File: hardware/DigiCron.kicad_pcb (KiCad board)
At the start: 2 copper layers, 36 x 36 mm, 11 parts, among them J100 Conn_Receptacle_2P, U100 MDBT50Q-U1MV2, U101 HCMS-3917, U102 HCMS-3917, U103 LTR-390UV-01, U104 ADXL345BCCZ-RL, U105 BME280, X100 12401598E4#2A

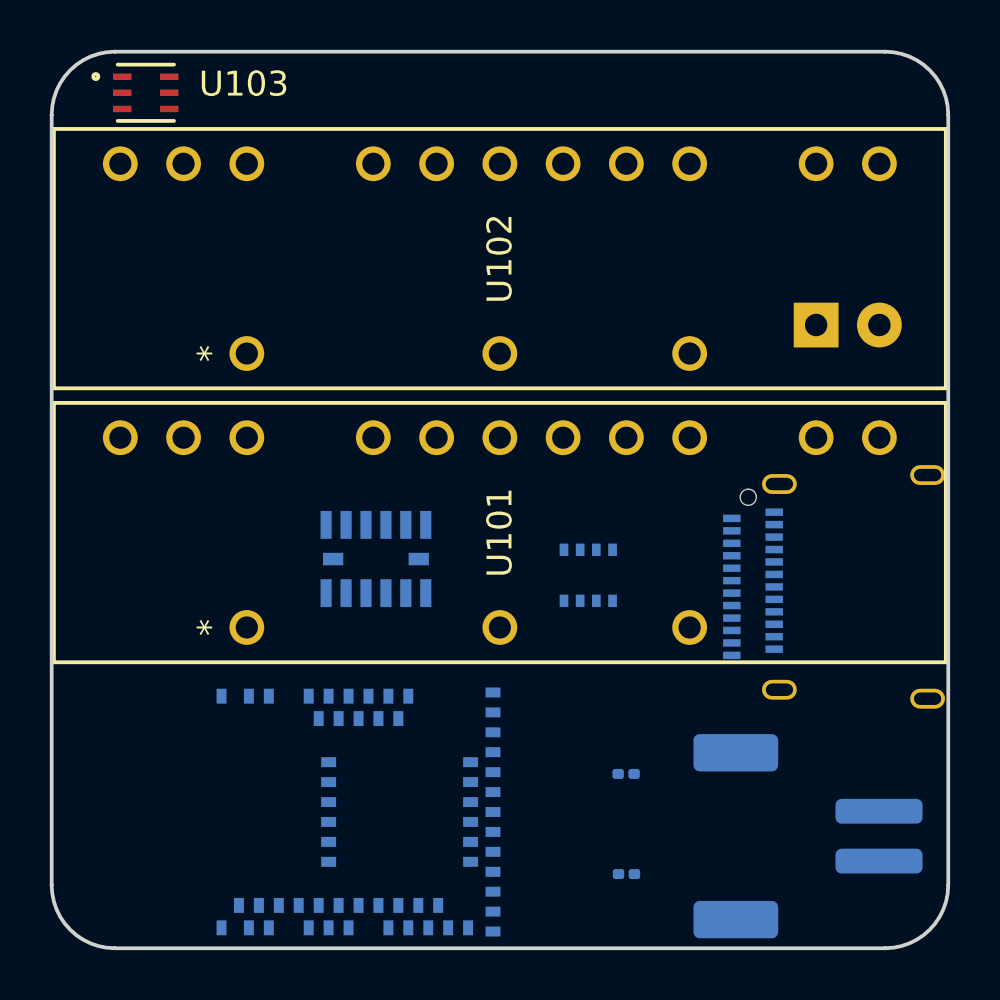
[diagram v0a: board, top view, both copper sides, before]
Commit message: Replace displays with 5V versions (due to supply availability) and add power management ICs
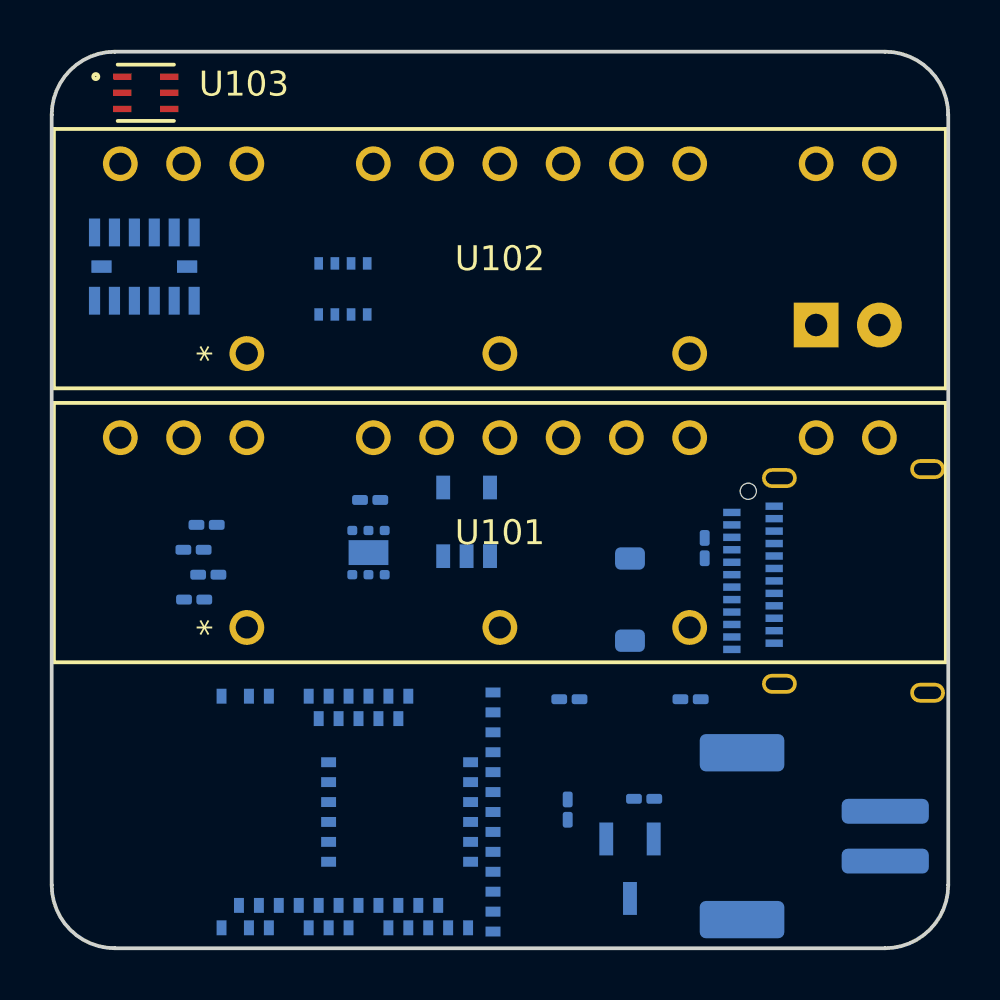
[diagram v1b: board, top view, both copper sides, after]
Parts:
- removed J100: Conn_Receptacle_2P, Connector_JST:JST_PH_S2B-PH-SM4-TB_1x02-1MP_P2.00mm_Horizontal
- removed R100, R101: 5.1K, Resistor_SMD:R_0201_0603Metric
- removed X100: 12401598E4#2A, USB-C:12401598E4#2A
- added C200: 10u, Capacitor_SMD:C_0201_0603Metric_Pad0.64x0.40mm_HandSolder, B.Cu at (203.7, 96.0)
- added C201: 10u, Capacitor_SMD:C_0201_0603Metric_Pad0.64x0.40mm_HandSolder, B.Cu at (186.1, 85.0)
- added C202: 10u, Capacitor_SMD:C_0201_0603Metric_Pad0.64x0.40mm_HandSolder, B.Cu at (185.6, 86.0)
- added C203: 10u, Capacitor_SMD:C_0201_0603Metric_Pad0.64x0.40mm_HandSolder, B.Cu at (186.2, 87.0)
- added C204: 10u, Capacitor_SMD:C_0201_0603Metric_Pad0.64x0.40mm_HandSolder, B.Cu at (185.6, 88.0)
- added D200: MBR0540, Diode_SMD:D_SOD-123, B.Cu at (203.1, 88.0)
- added J200: Conn_Receptacle_2P, Connector_JST:JST_PH_S2B-PH-SM4-TB_1x02-1MP_P2.00mm_Horizontal, B.Cu at (210.5, 97.5)
- added L200: 2.2u, Inductor_SMD:L_0201_0603Metric_Pad0.64x0.40mm_HandSolder, B.Cu at (192.7, 84.0)
- added Q200: AO3401A, AO3401A:SOT-23-3L_AOS, B.Cu at (203.1, 98.8)
- added R200: 5.1K, Resistor_SMD:R_0201_0603Metric_Pad0.64x0.40mm_HandSolder, B.Cu at (206.1, 86.0)
- added R201: 5.1K, Resistor_SMD:R_0201_0603Metric_Pad0.64x0.40mm_HandSolder, B.Cu at (205.6, 92.0)
- added R202: 100K, Resistor_SMD:R_0201_0603Metric_Pad0.64x0.40mm_HandSolder, B.Cu at (200.6, 96.5)
- added R203: 100K, Resistor_SMD:R_0201_0603Metric_Pad0.64x0.40mm_HandSolder, B.Cu at (200.7, 92.0)
- added U200: RT9080-33GJ5, RT9080:TSOT-23-5_RIT, B.Cu at (196.6, 84.9)
- added U201: TPS610997DRV, Package_SON:WSON-6-1EP_2x2mm_P0.65mm_EP1x1.6mm, B.Cu at (192.6, 86.2)
- added X200: 12401598E4#2A, USB-C:12401598E4#2A, B.Cu at (207.9, 87.3)
- moved U105 15.1 mm to (191.6, 75.6)
- moved U104 15.0 mm to (183.6, 74.7), turned to 90 degrees
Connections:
- net /A0 renamed A0
- net /A1 renamed A1
- net /A2 renamed A2
- net /A3 renamed A3
- net /A4 renamed A4
- net /A5 renamed A5
- net /ADPS_IRQ renamed ADPS_IRQ
- net /AREF renamed AREF
- net /D2 renamed D2
- net /HCMS_BLANK renamed HCMS_BLANK
- net /HCMS_CE renamed HCMS_CE
- net /HCMS_CLOCK renamed HCMS_CLOCK
- net /HCMS_DATA_IN renamed HCMS_DATA_IN
- net /HCMS_DATA_SHARE renamed HCMS_DATA_SHARE
- net /HCMS_RESET renamed HCMS_RESET
- net /HCMS_RS renamed HCMS_RS
- net /IR_IN renamed IR_IN
- net /JOY_BACK renamed JOY_BACK
- net /JOY_DOWN renamed JOY_DOWN
- net /JOY_HOME renamed JOY_HOME
- net /JOY_LEFT renamed JOY_LEFT
- net /JOY_RIGHT renamed JOY_RIGHT
- net /JOY_SELECT renamed JOY_SELECT
- net /JOY_UP renamed JOY_UP
- net /LED renamed LED
- net /MISO renamed MISO
- net /MOSI renamed MOSI
- net /QSPI_D0 renamed QSPI_D0
- net /QSPI_D1 renamed QSPI_D1
- net /QSPI_D2 renamed QSPI_D2
- net /QSPI_D3 renamed QSPI_D3
- net /QSPI_SCK renamed QSPI_SCK
- net /RESET renamed RESET
- net /RXD renamed RXD
- net /SCK renamed SCK
- net /SCL renamed SCL
- net /SDA renamed SDA
- net /SWCLK renamed SWCLK
- net /SWDIO renamed SWDIO
- net /TXD renamed TXD
- net /VDIV renamed VDIV
- D100 pad 1: GND -> unconnected-(D100-K-Pad1)
- D100 pad 2: /IR_OUT -> unconnected-(D100-A-Pad2)
- U100 pad 22: /IR_OUT -> IR_OUT
- U100 pad 34: /USB_D- -> USB_D-
- U100 pad 35: /USB_D+ -> USB_D+
- U100 pad 4: /D3 -> 5V_EN
- U101 pad 10: +3V3 -> +5V
- U101 pad 3: +3V3 -> +5V
- U102 pad 10: +3V3 -> +5V
- U102 pad 3: +3V3 -> +5V

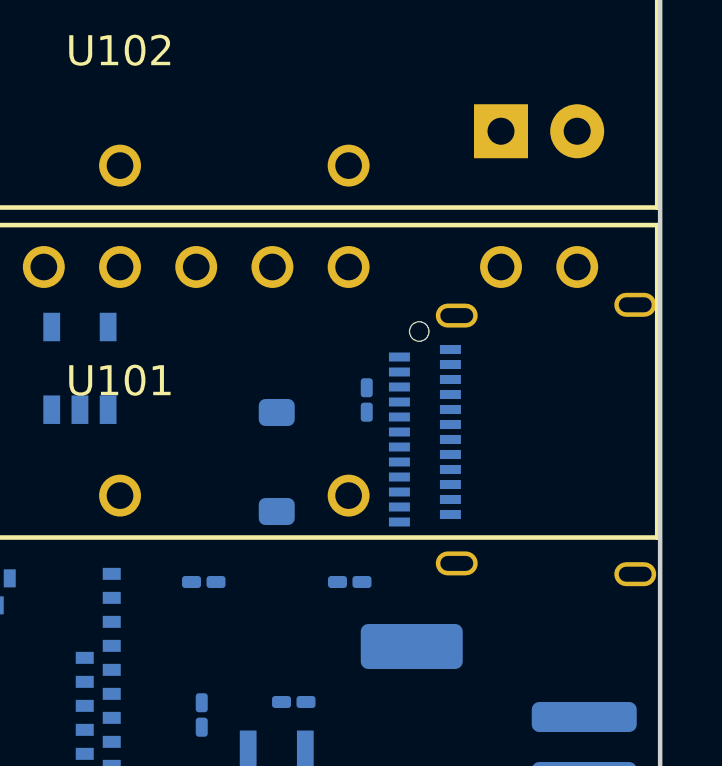
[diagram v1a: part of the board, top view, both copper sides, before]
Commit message: Change clearance to pass DRC for 0603 components
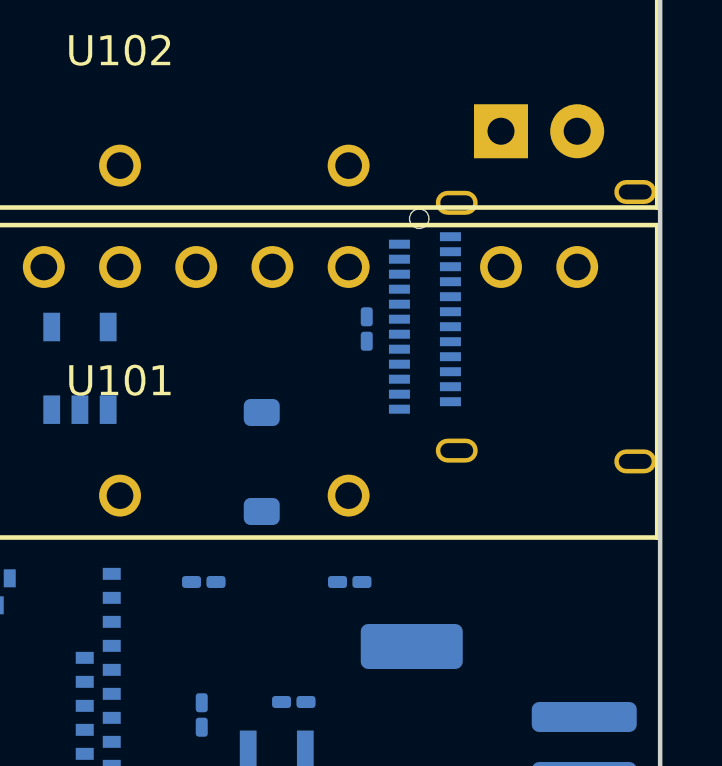
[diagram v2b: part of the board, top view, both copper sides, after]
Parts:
- moved X200 3.76 mm to (207.9, 83.5)
- moved R200 2.36 mm to (206.1, 83.6), turned to -90 degrees
- moved D200 0.50 mm to (202.6, 88.0)
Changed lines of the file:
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@@
 	)
 	(setup
+		(stackup
+			(layer "F.SilkS"
+				(type "Top Silk Screen")
+			)
+			(layer "F.Paste"
+				(type "Top Solder Paste")
+			)
+			(layer "F.Mask"
+				(type "Top Solder Mask")
+				(thickness 0.01)
+			)
+			(layer "F.Cu"
+				(type "copper")
+				(thickness 0.035)
+			)
+			(layer "dielectric 1"
+				(type "core")
+				(thickness 1.51)
+				(material "FR4")
+				(epsilon_r 4.5)
+				(loss_tangent 0.02)
+			)
+			(layer "B.Cu"
+				(type "copper")
+				(thickness 0.035)
+			)
+			(layer "B.Mask"
+				(type "Bottom Solder Mask")
+				(thickness 0.01)
+			)
+			(layer "B.Paste"
+				(type "Bottom Solder Paste")
+			)
+			(layer "B.SilkS"
+				(type "Bottom Silk Screen")
+			)
+			(copper_finish "None")
+			(dielectric_constraints no)
+		)
 		(pad_to_mask_clearance 0)
 		(allow_soldermask_bridges_in_footprints no)
@@
 		(sheetname "Power")
 		(sheetfile "Power.kicad_sch")
+		(clearance 0.15)
 		(attr smd)
 		(fp_line
@@
 		(sheetname "Power")
 		(sheetfile "Power.kicad_sch")
+		(clearance 0.15)
 		(attr smd)
 		(fp_line
@@
 	(footprint "Resistor_SMD:R_0201_0603Metric_Pad0.64x0.40mm_HandSolder"
 		(layer "B.Cu")
-		(at 206.12 85.9725 90)
+		(at 206.12 83.6075 -90)
 		(descr "Resistor SMD 0201 (0603 Metric), square (rectangular) end terminal, IPC_7351 nominal with elongated pad for handsoldering. (Body size source: https://www.vishay.com/docs/20052/crcw0201e3.pdf), generated with kicad-footprint-generator")
 		(tags "resistor handsolder")
 		(property "Reference" "R200"
-			(at 0.4325 -1 90)
+			(at 0.9325 1 90)
 			(layer "B.SilkS")
 			(effects
@@
 		)
 		(property "Footprint" "Resistor_SMD:R_0201_0603Metric_Pad0.64x0.40mm_HandSolder"
-			(at 0 0 -90)
+			(at 0 0 90)
 			(unlocked yes)
 			(layer "B.Fab")
@@
 		)
 		(property "Datasheet" ""
-			(at 0 0 -90)
+			(at 0 0 90)
 			(unlocked yes)
 			(layer "B.Fab")
@@
 		)
 		(property "Description" ""
-			(at 0 0 -90)
+			(at 0 0 90)
 			(unlocked yes)
 			(layer "B.Fab")
@@
 		(attr smd)
 		(fp_line
-			(start 0.88 -0.35)
-			(end 0.88 0.35)
+			(start -0.88 0.35)
+			(end -0.88 -0.35)
 			(stroke
 				(width 0.05)
@@
 		)
 		(fp_line
-			(start -0.88 -0.35)
-			(end 0.88 -0.35)
+			(start 0.88 0.35)
+			(end -0.88 0.35)
 			(stroke
 				(width 0.05)
@@
 		)
 		(fp_line
-			(start 0.88 0.35)
-			(end -0.88 0.35)
+			(start -0.88 -0.35)
+			(end 0.88 -0.35)
 			(stroke
 				(width 0.05)
@@
 		)
 		(fp_line
-			(start -0.88 0.35)
-			(end -0.88 -0.35)
+			(start 0.88 -0.35)
+			(end 0.88 0.35)
 			(stroke
 				(width 0.05)
@@
 		)
 		(fp_line
-			(start 0.3 -0.15)
-			(end 0.3 0.15)
+			(start -0.3 0.15)
+			(end -0.3 -0.15)
 			(stroke
 				(width 0.1)
@@
 		)
 		(fp_line
-			(start -0.3 -0.15)
-			(end 0.3 -0.15)
+			(start 0.3 0.15)
+			(end -0.3 0.15)
 			(stroke
 				(width 0.1)
@@
 		)
 		(fp_line
-			(start 0.3 0.15)
-			(end -0.3 0.15)
+			(start -0.3 -0.15)
+			(end 0.3 -0.15)
 			(stroke
 				(width 0.1)
@@
 		)
 		(fp_line
-			(start -0.3 0.15)
-			(end -0.3 -0.15)
+			(start 0.3 -0.15)
+			(end 0.3 0.15)
 			(stroke
 				(width 0.1)
@@
 		)
 		(pad "" smd roundrect
-			(at -0.4325 0 90)
+			(at -0.4325 0 270)
 			(size 0.458 0.36)
 			(layers "B.Paste")
@@
 		)
 		(pad "" smd roundrect
-			(at 0.4325 0 90)
+			(at 0.4325 0 270)
 			(size 0.458 0.36)
 			(layers "B.Paste")
@@
 		)
 		(pad "1" smd roundrect
-			(at -0.4075 0 90)
+			(at -0.4075 0 270)
 			(size 0.635 0.4)
 			(layers "B.Cu" "B.Mask")
@@
 		)
 		(pad "2" smd roundrect
-			(at 0.4075 0 90)
+			(at 0.4075 0 270)
 			(size 0.635 0.4)
 			(layers "B.Cu" "B.Mask")
@@
 		(tags "capacitor handsolder")
 		(property "Reference" "C201"
-			(at 3.0675 0 0)
+			(at 3.0675 0 180)
 			(layer "B.SilkS")
 			(effects
@@
 		)
 		(property "Value" "10u"
-			(at 0 -1.05 0)
+			(at 0 -1.05 180)
 			(layer "B.Fab")
 			(effects
@@
 		(sheetname "Power")
 		(sheetfile "Power.kicad_sch")
+		(clearance 0.15)
 		(attr smd)
 		(fp_line
@@
 		)
 		(fp_text user "${REFERENCE}"
-			(at 0 0.68 0)
+			(at 0 0.68 180)
 			(layer "B.Fab")
 			(effects
@@
 	(footprint "Diode_SMD:D_SOD-123"
 		(layer "B.Cu")
-		(at 203.12 88.04 90)
+		(at 202.62 88.04 90)
 		(descr "SOD-123")
 		(tags "SOD-123")
@@
 	(footprint "USB-C:12401598E4#2A"
 		(layer "B.Cu")
-		(at 207.87 87.29 -90)
+		(at 207.87 83.53 -90)
 		(property "Reference" "X200"
 			(at -0.25 -4.25 0)
@@
 		(sheetname "Power")
 		(sheetfile "Power.kicad_sch")
+		(clearance 0.15)
 		(attr smd)
 		(fp_line

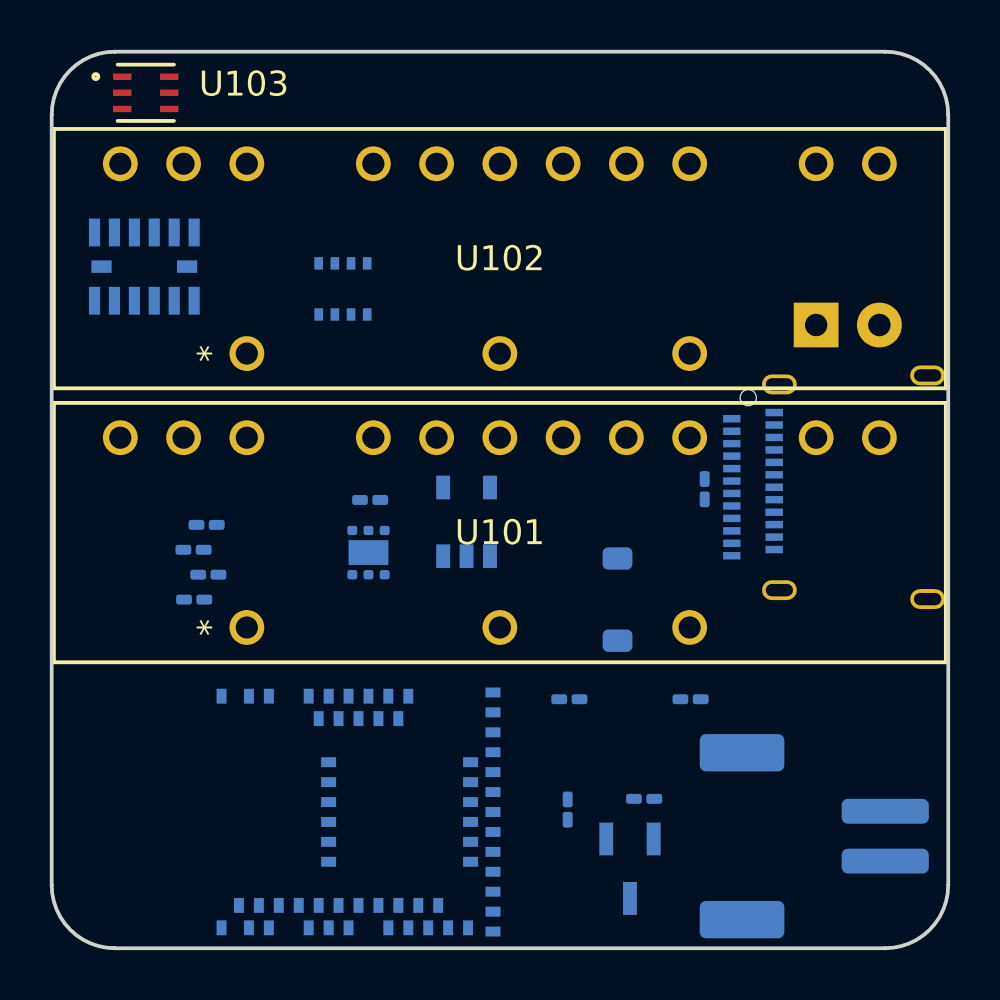
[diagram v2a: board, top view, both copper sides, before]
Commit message: Modify 5V boost converter to use VBAT instead of 3V3 for input and add power switching circuit
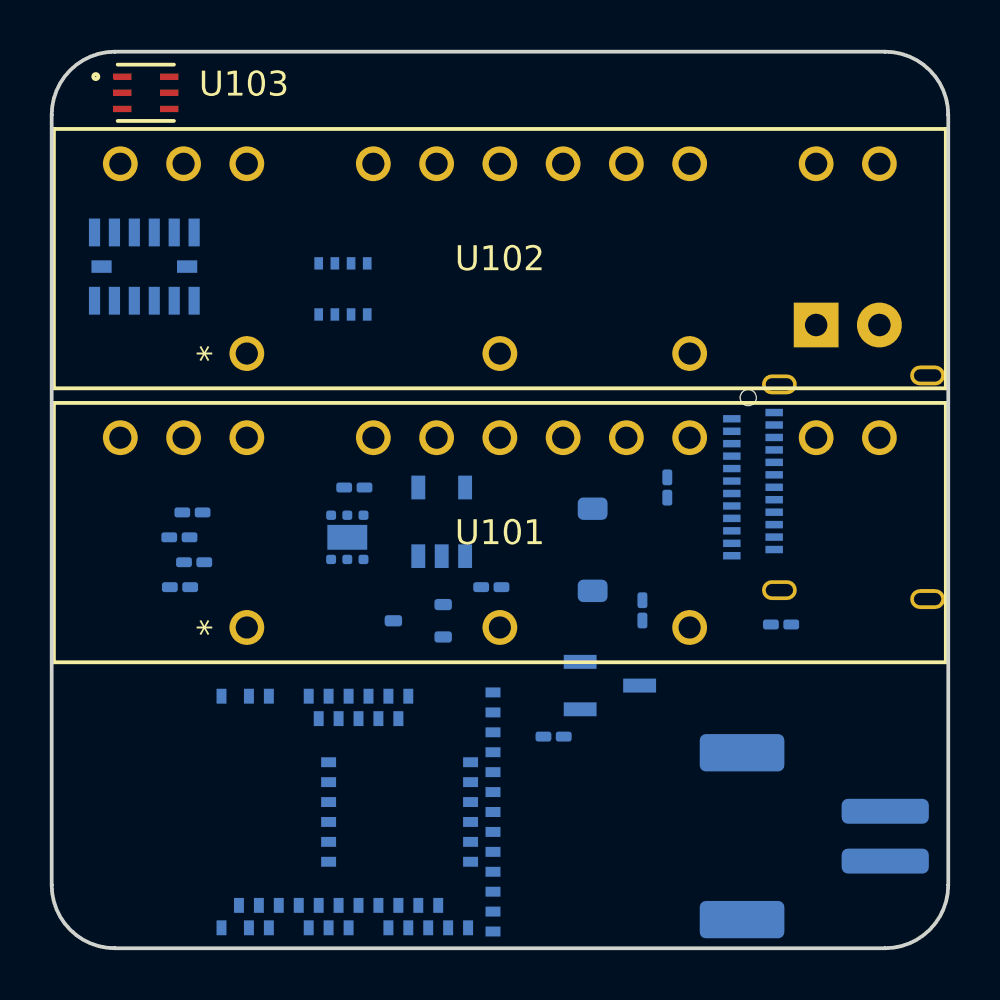
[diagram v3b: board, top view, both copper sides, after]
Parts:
- added D201: BAT54CW, Package_TO_SOT_SMD:SOT-323_SC-70, B.Cu at (194.6, 88.9)
- moved C200 7.57 mm to (203.6, 88.5), turned to 90 degrees
- moved Q200 7.40 mm to (202.3, 91.5), turned to 90 degrees
- moved R203 5.48 mm to (197.6, 87.5)
- moved R201 4.71 mm to (209.2, 89.0)
- moved R202 2.99 mm to (200.1, 93.5), turned to 180 degrees
- moved D200 2.24 mm to (201.6, 86.0)
- moved R200 1.50 mm to (204.6, 83.5)
- moved U201 1.05 mm to (191.8, 85.5)
- moved U200 1.00 mm to (195.6, 84.9)
- moved L200 0.81 mm to (192.1, 83.5)
- moved C201 0.76 mm to (185.6, 84.5)
- moved C202 0.76 mm to (185.0, 85.5)
- moved C203 0.76 mm to (185.6, 86.5)
- moved C204 0.76 mm to (185.1, 87.5)
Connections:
- C202 pad 2: +3V3 -> VBAT
- C203 pad 1: +5V -> Net-(U201-VOUT)
- C204 pad 1: +5V -> Net-(U201-VOUT)
- J200 pad 1: unconnected-(J200-L-Pad1) -> VBAT
- J200 pad 2: unconnected-(J200-N-Pad2) -> GND
- L200 pad 1: +3V3 -> VBAT
- U101 pad 21: +3V3 -> +5V
- U101 pad 22: +3V3 -> +5V
- U102 pad 21: +3V3 -> +5V
- U102 pad 22: +3V3 -> +5V
- U201 pad 2: +5V -> Net-(U201-VOUT)
- U201 pad 6: +3V3 -> VBAT
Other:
- board text added: "+"

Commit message: Add pads for wiring vibration motor and piezo buzzer
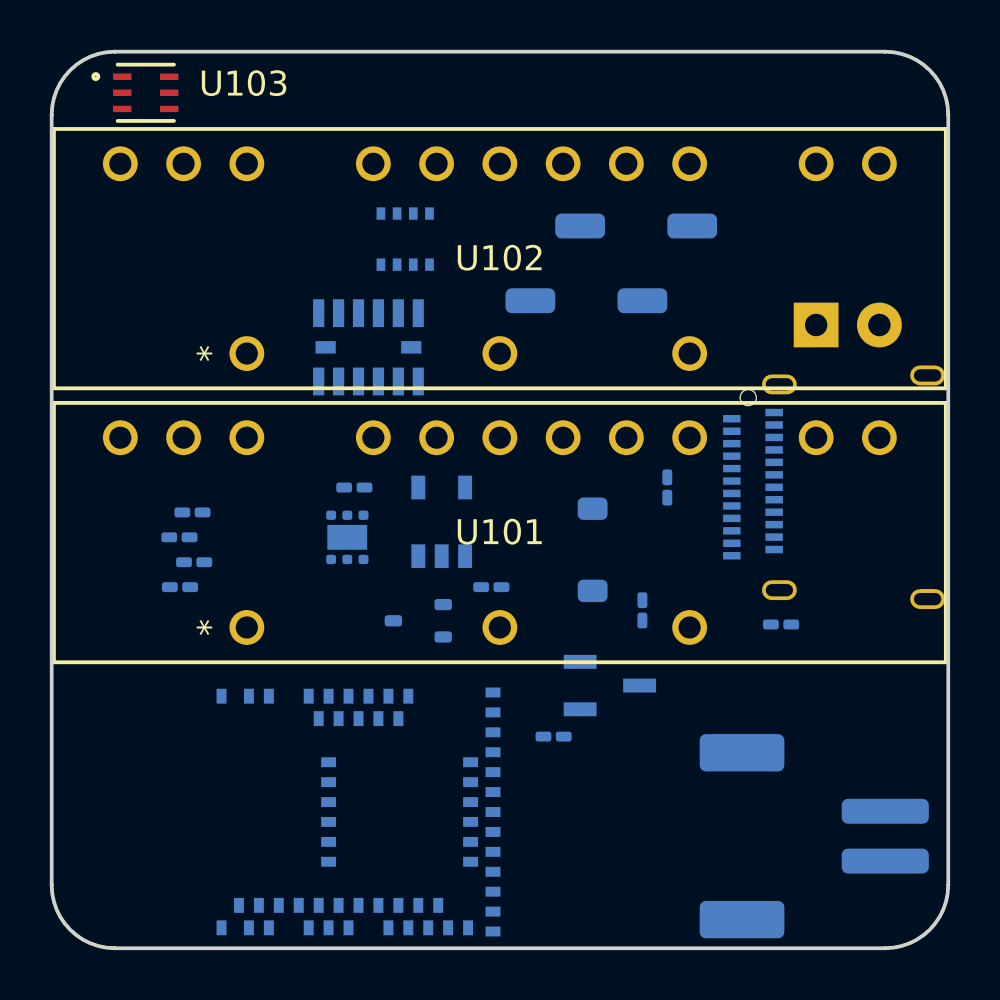
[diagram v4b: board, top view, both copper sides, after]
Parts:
- added J100: Solder pad, Connector_Wire:SolderWirePad_1x01_SMD_1x2mm, B.Cu at (205.6, 73.0)
- added J101: Solder pad, Connector_Wire:SolderWirePad_1x01_SMD_1x2mm, B.Cu at (203.6, 76.0)
- added J102: Solder pad, Connector_Wire:SolderWirePad_1x01_SMD_1x2mm, B.Cu at (201.1, 73.0)
- added J103: Solder pad, Connector_Wire:SolderWirePad_1x01_SMD_1x2mm, B.Cu at (199.1, 76.0)
- moved U104 9.57 mm to (192.6, 77.9), turned to -90 degrees
- moved U105 3.20 mm to (194.1, 73.6)
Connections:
- U100 pad 11: A4 -> VIBMOTOR
- U100 pad 9: A5 -> PIEZO
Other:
- board text added: "M+"
- board text added: "M-"
- board text added: "P+"
- board text added: "P-"
